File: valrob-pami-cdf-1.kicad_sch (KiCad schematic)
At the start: 123 parts, among them J1 Conn_01x04, J2 USB_C_Receptacle_USB2.0_14P, J3 Conn_01x02, J4 Conn_01x04_Pin, M1 Motor_Servo, Q1 Q_NMOS, Q2 Q_NMOS, Q3 Q_NMOS, SW1 SW_SPST, SW2 SW_Push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

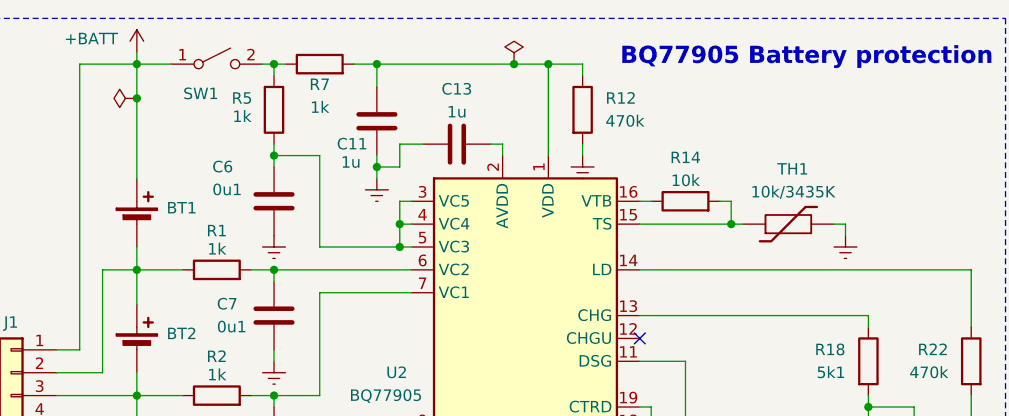
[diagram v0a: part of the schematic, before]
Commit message: pcb: add bms layout
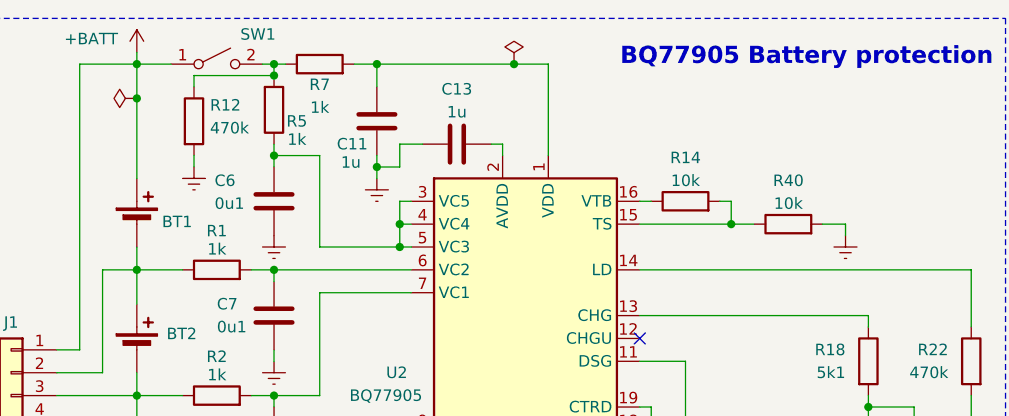
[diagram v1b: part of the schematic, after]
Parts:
- removed TH1: 10k/3435K, Connector_JST:JST_PH_B2B-PH-K_1x02_P2.00mm_Vertical, symbol Device:Thermistor
- added R40: 10k, Resistor_SMD:R_0402_1005Metric, symbol Device:R
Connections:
- net BGND: now also R40.2
- net at R14.2, U2.15 (TS): now also R40.1
- net at C11.2, R7.2, U2.1 (VDD): no longer R12.1
- net at R5.2, R7.1, SW1.2 (B): now also R12.1
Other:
- moved on the sheet: R12

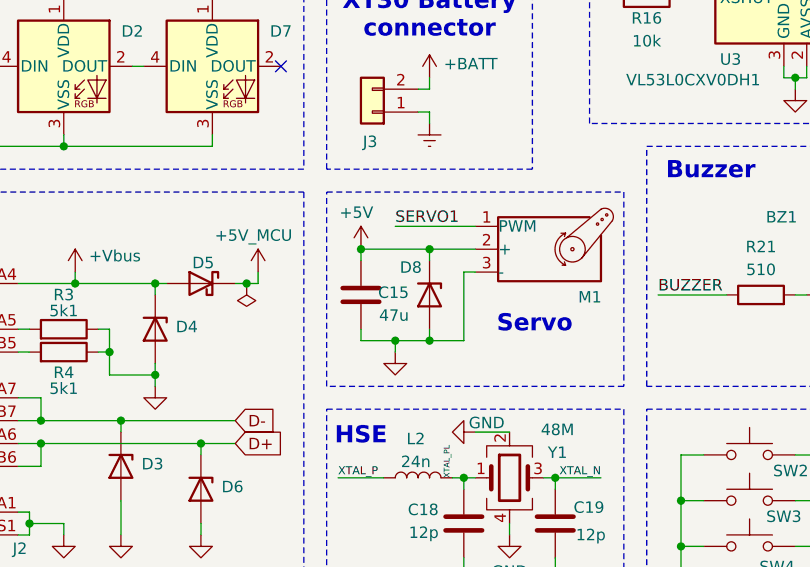
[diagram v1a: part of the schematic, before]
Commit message: pcb: refine layout and add board outline
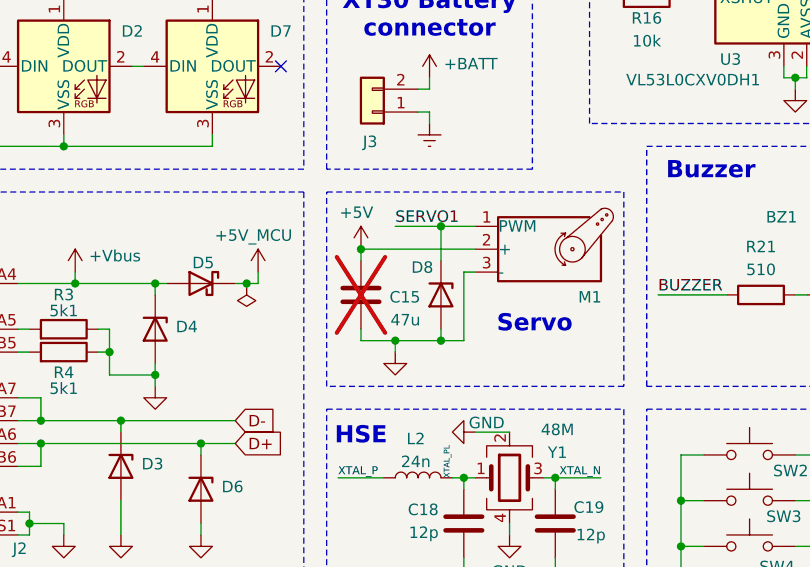
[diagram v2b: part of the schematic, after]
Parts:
- C15: now not fitted
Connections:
- net +5V: no longer D8.1 (K)
- net SERVO1: now also D8.1 (K)
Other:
- moved on the sheet: D8
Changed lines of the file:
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@@
 	)
 	(junction
-		(at 85.09 167.64)
-		(diameter 0)
-		(color 0 0 0 0)
-	)
-	(junction
 		(at 212.09 20.32)
 		(diameter 0)
@@
 	)
 	(junction
+		(at 86.36 154.94)
+		(diameter 0)
+		(color 0 0 0 0)
+	)
+	(junction
 		(at 25.4 95.25)
 		(diameter 0)
@@
 	)
 	(junction
-		(at 85.09 157.48)
+		(at 176.53 44.45)
 		(diameter 0)
 		(color 0 0 0 0)
 	)
 	(junction
-		(at 176.53 44.45)
+		(at 86.36 167.64)
 		(diameter 0)
 		(color 0 0 0 0)
@@
 	(wire
 		(pts
-			(xy 77.47 157.48) (xy 85.09 157.48)
-		)
-		(stroke
-			(width 0)
-			(type default)
-		)
-	)
-	(wire
-		(pts
 			(xy 134.62 167.64) (xy 134.62 168.91)
 		)
@@
 	(wire
 		(pts
-			(xy 81.28 167.64) (xy 85.09 167.64)
+			(xy 81.28 167.64) (xy 86.36 167.64)
 		)
 		(stroke
@@
 	(wire
 		(pts
-			(xy 85.09 157.48) (xy 85.09 158.75)
-		)
-		(stroke
-			(width 0)
-			(type default)
-		)
-	)
-	(wire
-		(pts
 			(xy 40.64 187.96) (xy 44.45 187.96)
 		)
@@
 	(wire
 		(pts
-			(xy 88.9 167.64) (xy 85.09 167.64)
+			(xy 88.9 167.64) (xy 86.36 167.64)
 		)
 		(stroke
@@
 	(wire
 		(pts
-			(xy 85.09 157.48) (xy 90.17 157.48)
+			(xy 77.47 157.48) (xy 90.17 157.48)
 		)
 		(stroke
@@
 	(wire
 		(pts
+			(xy 86.36 154.94) (xy 86.36 158.75)
+		)
+		(stroke
+			(width 0)
+			(type default)
+		)
+	)
+	(wire
+		(pts
 			(xy 242.57 149.86) (xy 242.57 147.32)
 		)
@@
 	(wire
 		(pts
+			(xy 86.36 154.94) (xy 90.17 154.94)
+		)
+		(stroke
+			(width 0)
+			(type default)
+		)
+	)
+	(wire
+		(pts
 			(xy 90.17 57.15) (xy 88.9 57.15)
 		)
@@
 	(wire
 		(pts
-			(xy 81.28 154.94) (xy 90.17 154.94)
+			(xy 81.28 154.94) (xy 86.36 154.94)
 		)
 		(stroke
@@
 	(wire
 		(pts
-			(xy 85.09 166.37) (xy 85.09 167.64)
+			(xy 86.36 166.37) (xy 86.36 167.64)
 		)
 		(stroke
@@
 	(symbol
 		(lib_id "GLCS:H5VU10U")
-		(at 85.09 162.56 270)
+		(at 86.36 162.56 270)
 		(unit 1)
 		(exclude_from_sim no)
@@
 		(dnp no)
 		(property "Reference" "D8"
-			(at 81.788 159.512 90)
+			(at 83.058 159.512 90)
 			(effects
 				(font
@@
 		)
 		(property "Value" "H5VU10U"
-			(at 87.63 163.8299 90)
+			(at 88.9 163.8299 90)
 			(effects
 				(font
@@
 		)
 		(property "Footprint" "GLCS:Diode_DFN1006"
-			(at 80.645 162.56 0)
+			(at 81.915 162.56 0)
 			(effects
 				(font
@@
 		)
 		(property "Datasheet" "https://datasheet.lcsc.com/lcsc/2504101957_hongjiacheng-H5VU10U_C22395519.pdf"
-			(at 85.09 162.56 0)
+			(at 86.36 162.56 0)
 			(effects
 				(font
@@
 		)
 		(property "Description" "-55℃~+155℃ 0.8pF 16V 200nA 55W@8/20us 5A@8/20us 5V 6V ESD IEC 61000-4-2 Unidirectional DFN1006-2L ESD and Surge Protection (TVS/ESD) ROHS"
-			(at 85.09 162.56 0)
+			(at 86.36 162.56 0)
 			(effects
 				(font
@@
 		)
 		(property "Basic" "E"
-			(at 85.09 162.56 90)
+			(at 86.36 162.56 90)
 			(effects
 				(font
@@
 		)
 		(property "JLCPCB Part #" "C22395519"
-			(at 85.09 162.56 90)
+			(at 86.36 162.56 90)
 			(effects
 				(font
@@
 		)
 		(property "Manufacturer" "hongjiacheng"
-			(at 85.09 162.56 90)
+			(at 86.36 162.56 90)
 			(effects
 				(font
@@
 		)
 		(property "Manufacturer Part Number" "H5VU10U"
-			(at 85.09 162.56 90)
+			(at 86.36 162.56 90)
 			(effects
 				(font
@@
 		(in_bom yes)
 		(on_board yes)
-		(dnp no)
+		(dnp yes)
 		(property "Reference" "C15"
-			(at 82.804 162.306 0)
+			(at 84.074 162.814 0)
 			(effects
 				(font
@@
 		)
 		(property "Value" "47u"
-			(at 82.804 164.846 0)
+			(at 84.074 165.354 0)
 			(effects
 				(font

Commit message: schem: update connectors to horizontal footprints
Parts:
- J1: footprint Connector_JST:JST_XH_B4B-XH-A_1x04_P2.50mm_Vertical -> Connector_JST:JST_XH_S4B-XH-A_1x04_P2.50mm_Horizontal; JLCPCB Part # C144395 -> (none); Manufacturer Part Number B4B-XH-A(LF)(SN) -> (none)
- J3: footprint Connector_AMASS:AMASS_XT30U-M_1x02_P5.0mm_Vertical -> Connector_AMASS:AMASS_XT30PW-M_1x02_P2.50mm_Horizontal; JLCPCB Part # C99101 -> C431092; Manufacturer Part Number XT30U-M -> XT30PW-M30.G.Y
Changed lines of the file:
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@@
 			)
 		)
-		(property "Footprint" "Connector_JST:JST_XH_B4B-XH-A_1x04_P2.50mm_Vertical"
+		(property "Footprint" "Connector_JST:JST_XH_S4B-XH-A_1x04_P2.50mm_Horizontal"
 			(at 19.05 53.34 0)
 			(effects
@@
 			)
 		)
-		(property "JLCPCB Part #" "C144395"
+		(property "JLCPCB Part #" ""
 			(at 19.05 53.34 0)
 			(effects
@@
 			)
 		)
-		(property "Manufacturer Part Number" "B4B-XH-A(LF)(SN)"
+		(property "Manufacturer Part Number" ""
 			(at 19.05 53.34 0)
 			(effects
@@
 			)
 		)
-		(property "Footprint" "Connector_AMASS:AMASS_XT30U-M_1x02_P5.0mm_Vertical"
+		(property "Footprint" "Connector_AMASS:AMASS_XT30PW-M_1x02_P2.50mm_Horizontal"
 			(at 78.74 142.24 0)
 			(effects
@@
 			)
 		)
-		(property "JLCPCB Part #" "C99101"
+		(property "JLCPCB Part #" "C431092"
 			(at 78.74 142.24 0)
 			(effects
@@
 			)
 		)
-		(property "Manufacturer Part Number" "XT30U-M"
+		(property "Manufacturer Part Number" "XT30PW-M30.G.Y"
 			(at 78.74 142.24 0)
 			(effects

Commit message: schem: update servo connector to horizontal
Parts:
- M1: footprint Connector_PinHeader_2.54mm:PinHeader_1x03_P2.54mm_Vertical -> Connector_PinHeader_2.54mm:PinHeader_1x03_P2.54mm_Horizontal
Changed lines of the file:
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@@
 			)
 		)
-		(property "Footprint" "Connector_PinHeader_2.54mm:PinHeader_1x03_P2.54mm_Vertical"
+		(property "Footprint" "Connector_PinHeader_2.54mm:PinHeader_1x03_P2.54mm_Horizontal"
 			(at 97.79 162.306 0)
 			(effects

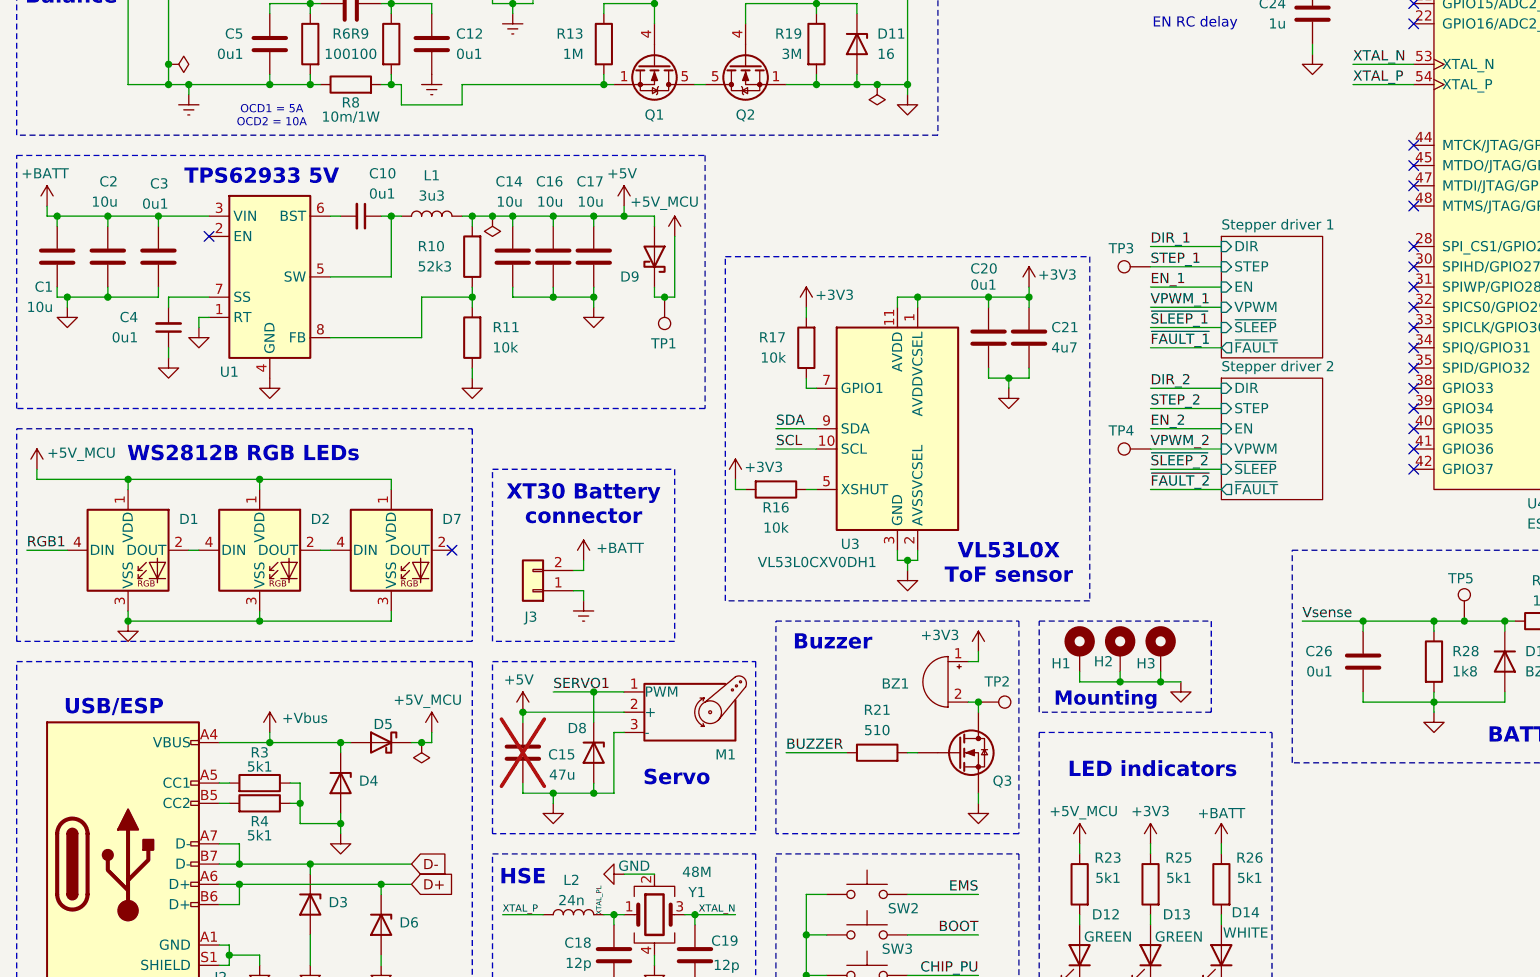
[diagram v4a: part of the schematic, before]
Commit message: pcb: change connectors layout
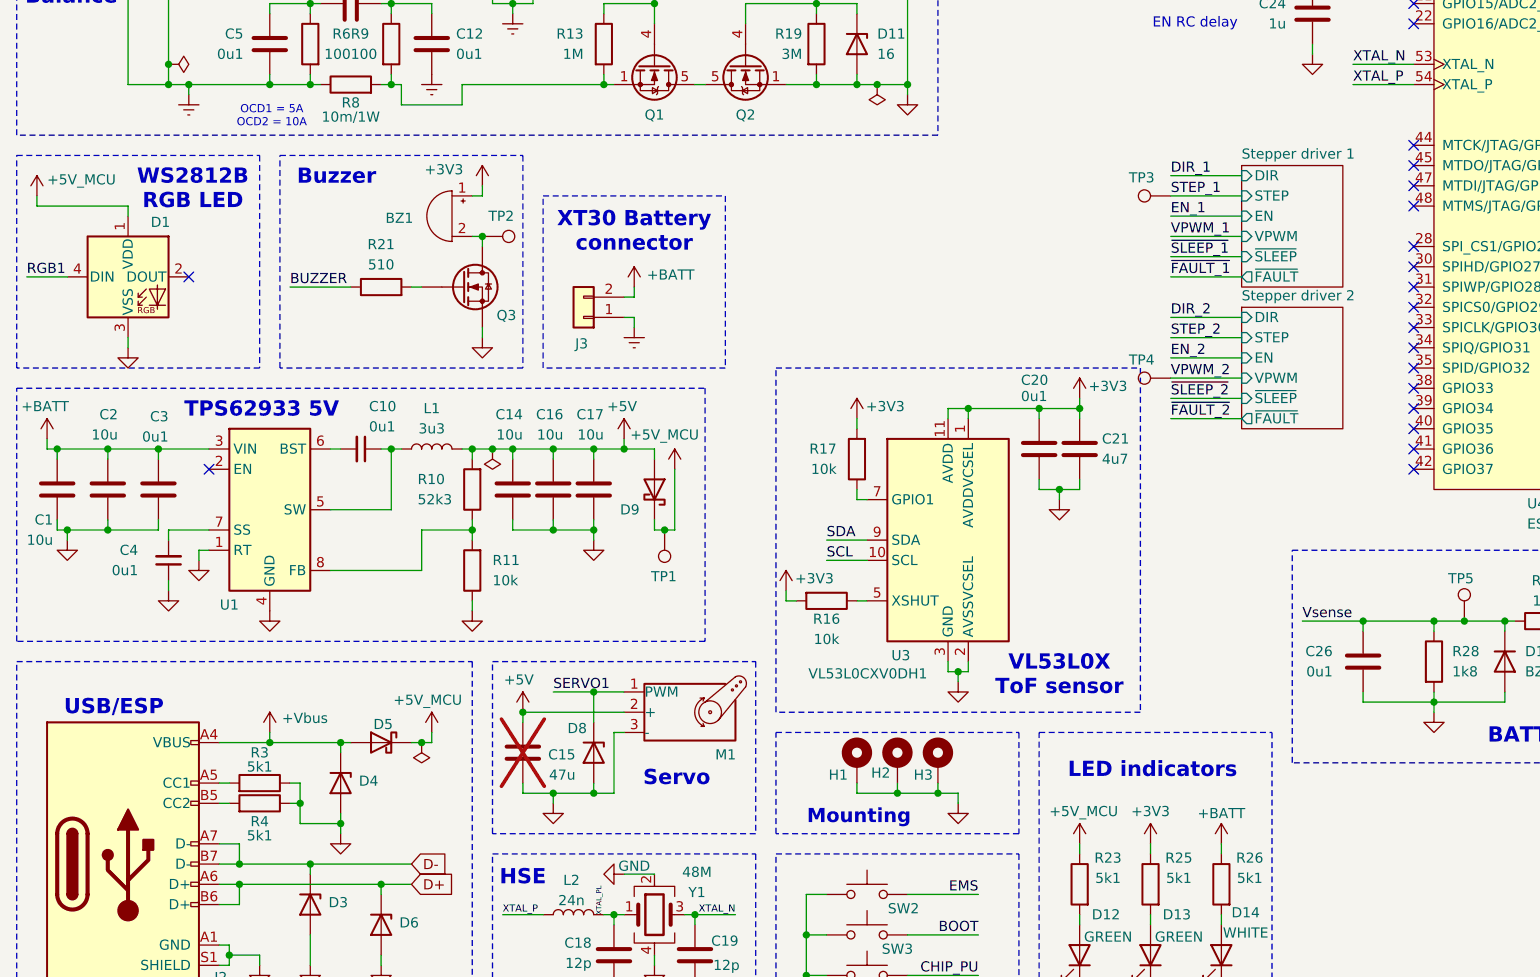
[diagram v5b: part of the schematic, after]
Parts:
- removed D2, D7: WS2812B, LED_SMD:LED_WS2812B_PLCC4_5.0x5.0mm_P3.2mm, symbol LED:WS2812B
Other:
- note added: "WS2812B RGB LED"
- note removed: "WS2812B RGB LEDs"
- moved on the sheet: BZ1, C1, C10, C14, C16, C17, C2, C20, C21, C3, C4, D1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

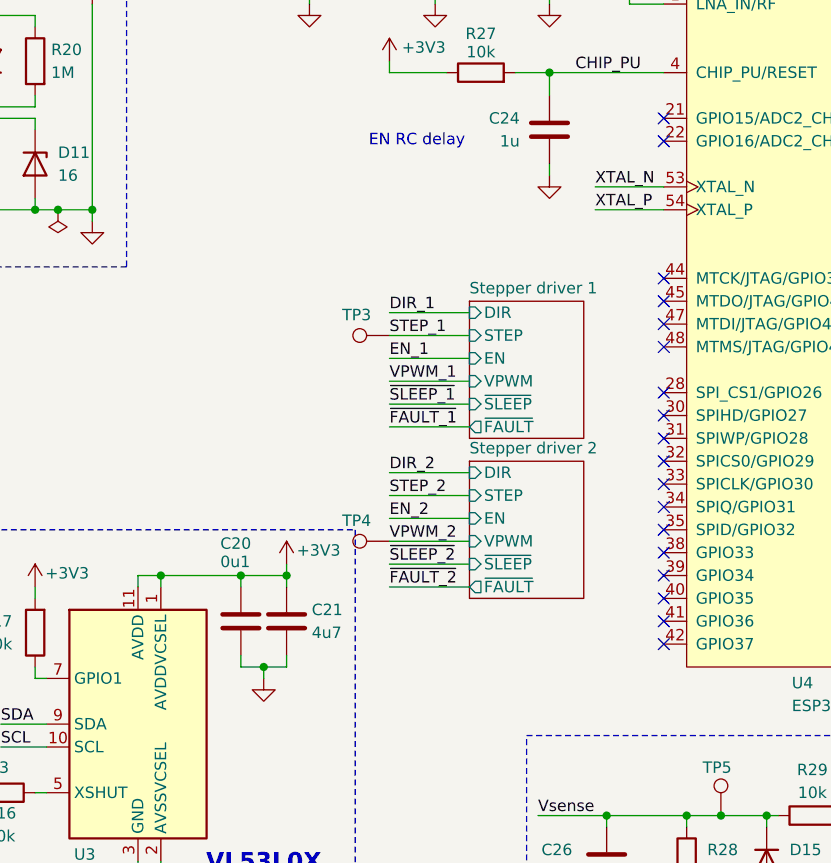
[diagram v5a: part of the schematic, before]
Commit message: schem: add 6 spare gpio header
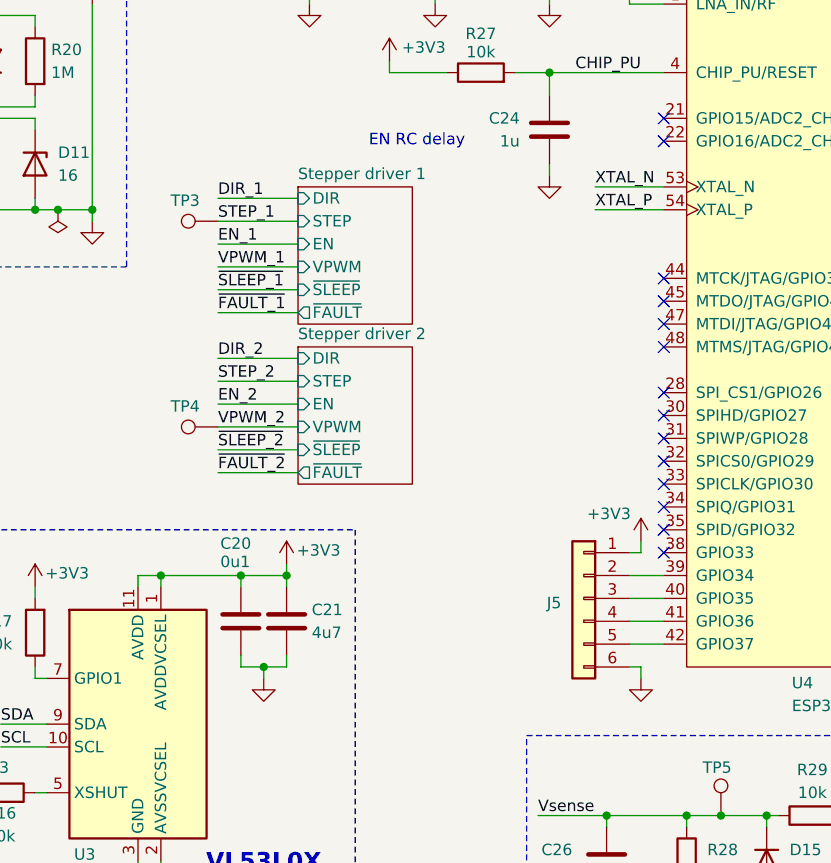
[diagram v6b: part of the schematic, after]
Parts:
- added J5: Conn_01x06, Connector_PinHeader_2.54mm:PinHeader_2x03_P2.54mm_Vertical, symbol Connector_Generic:Conn_01x06
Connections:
- net +3V3: now also J5.1 (Pin_1)
- net GND: now also J5.6 (Pin_6)
- net at U4.39 (GPIO34): now also J5.2 (Pin_2)
- net at U4.40 (GPIO35): now also J5.3 (Pin_3)
- net at U4.41 (GPIO36): now also J5.4 (Pin_4)
- net at U4.42 (GPIO37): now also J5.5 (Pin_5)
- no-connect marks 24 -> 20
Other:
- moved on the sheet: TP3, TP4
